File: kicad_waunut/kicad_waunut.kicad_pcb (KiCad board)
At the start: 2 copper layers, 129.3 x 265.9 mm, 76 parts, among them J1 Conn_01x06_Pin, J2 Conn_01x02_Pin, U1 ATtiny861A-S

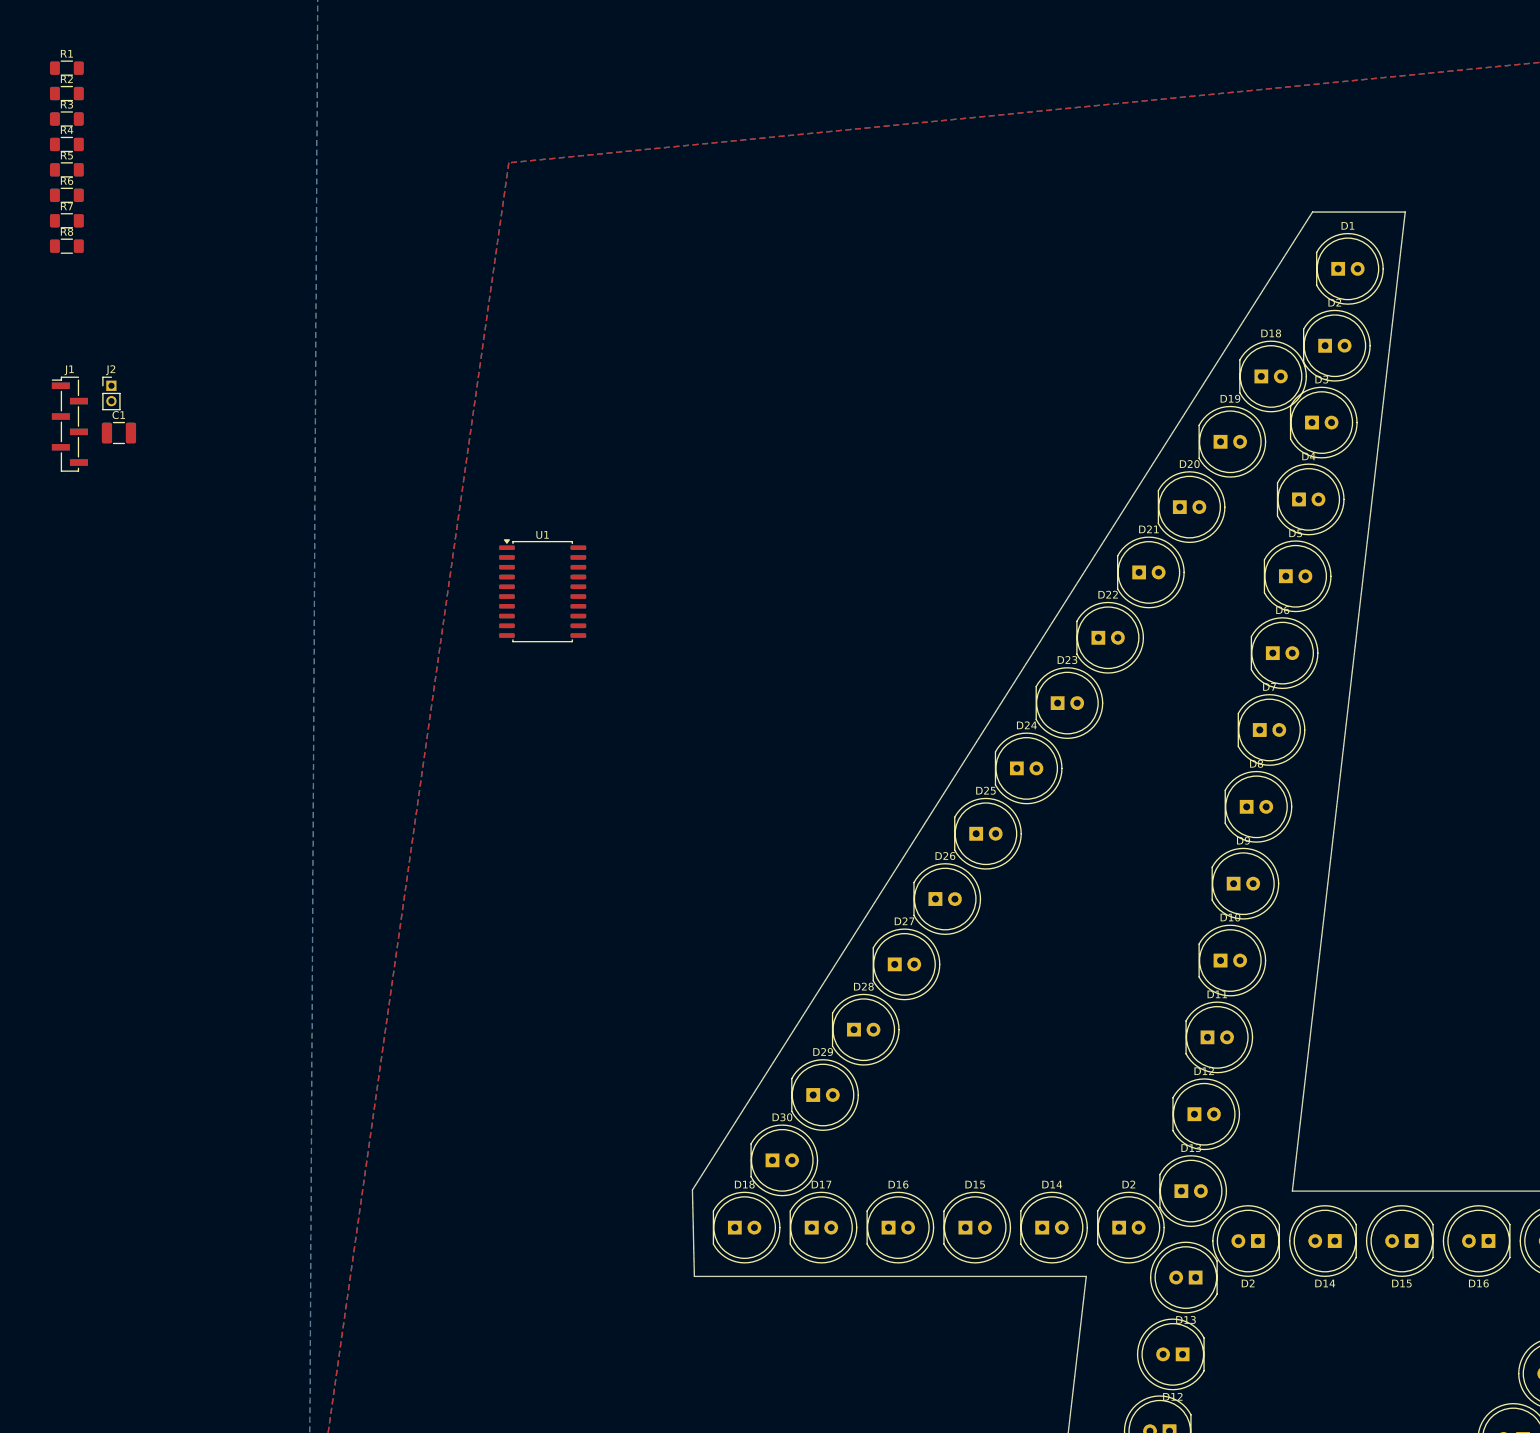
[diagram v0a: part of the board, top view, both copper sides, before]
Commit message: 2 lediä vilkkuu - vilkutus_2x.c
Jostain syystä kummallinen if statementti jossa 2 lediä palaa mutta eri
kirrkaudella.

Muutama ledi himmenee/kirkastuu. hmm...

Muuten jeba
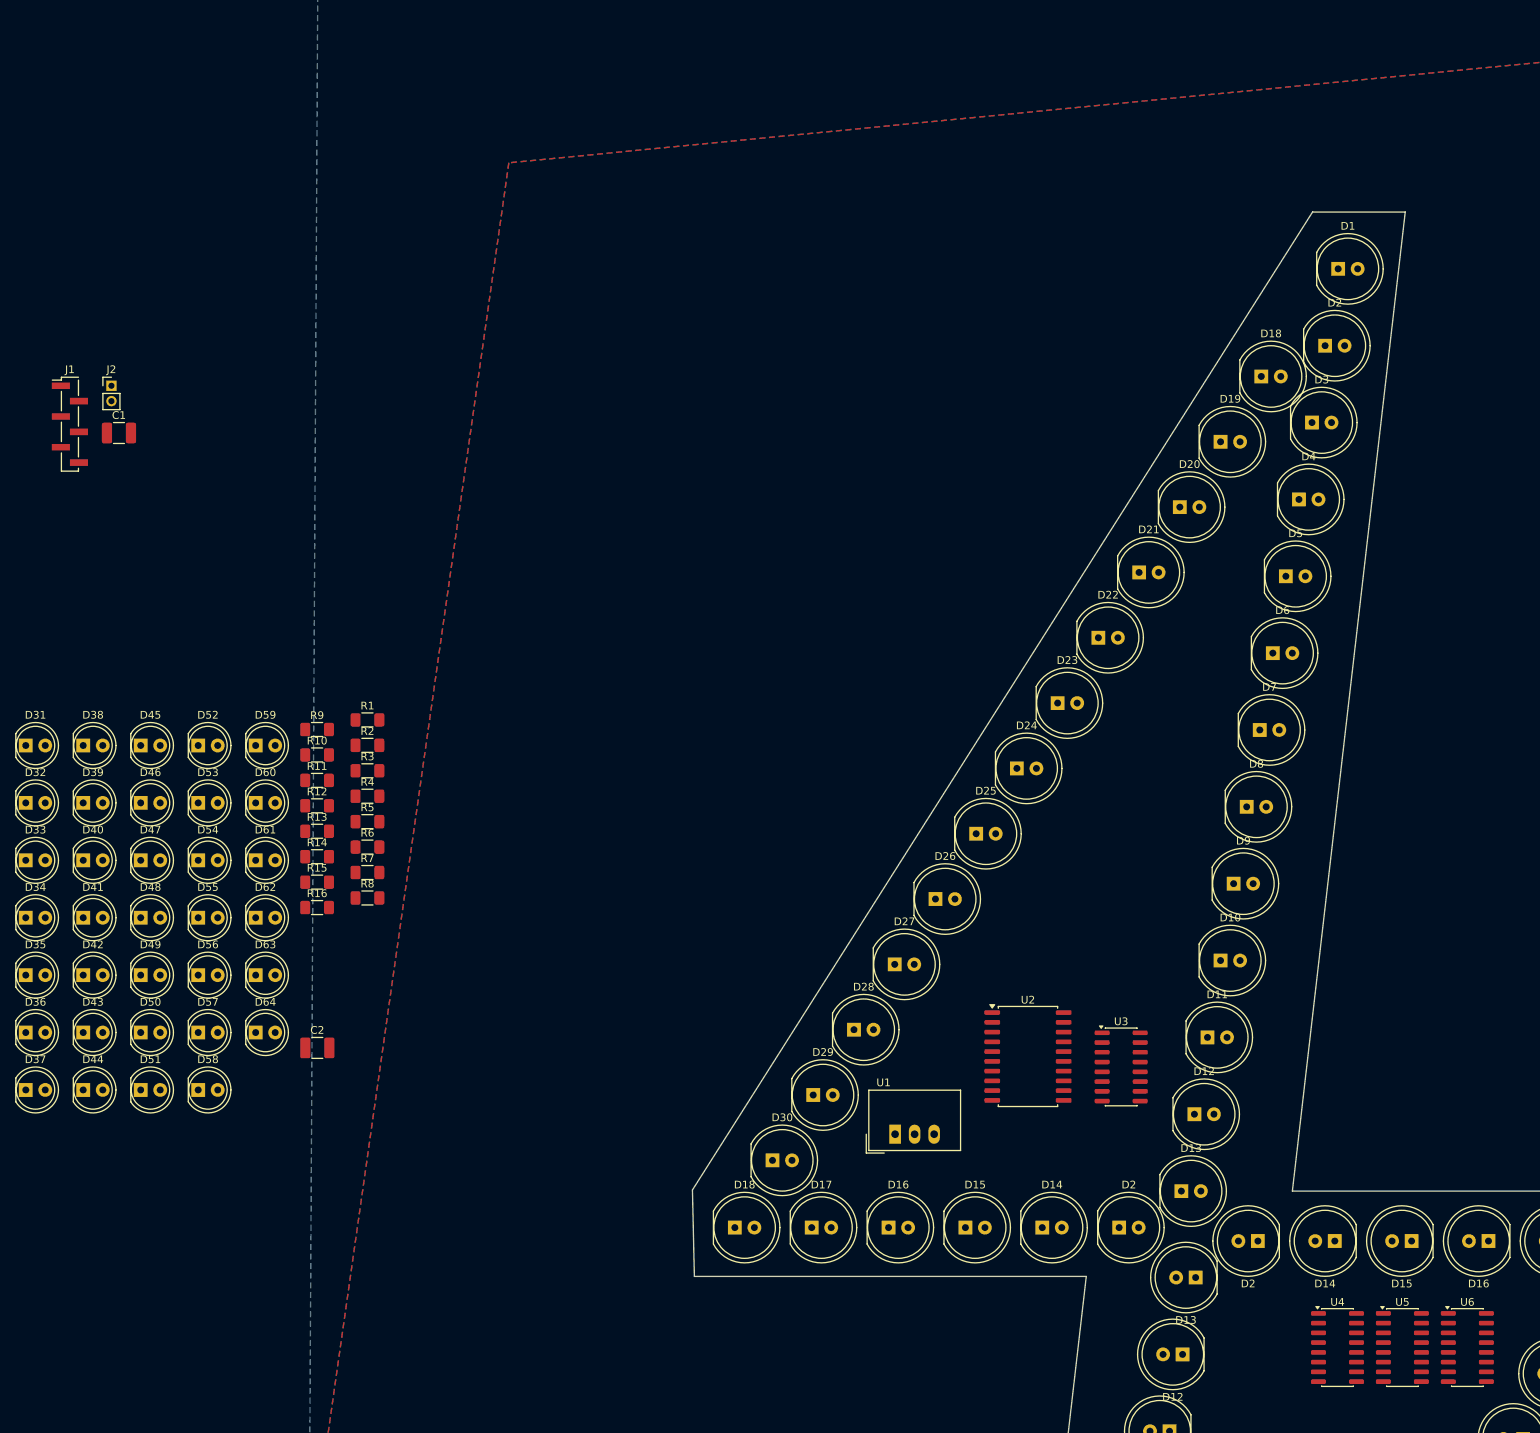
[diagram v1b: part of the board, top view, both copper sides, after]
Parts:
- added C2: 10 u, Capacitor_SMD:C_1210_3225Metric_Pad1.33x2.70mm_HandSolder, F.Cu at (15.9, 148.4)
- added D31: LED, LED_THT:LED_D5.0mm, F.Cu at (-22.1, 109.0)
- added D32: LED, LED_THT:LED_D5.0mm, F.Cu at (-22.1, 116.5)
- added D33: LED, LED_THT:LED_D5.0mm, F.Cu at (-22.1, 124.0)
- added D34: LED, LED_THT:LED_D5.0mm, F.Cu at (-22.1, 131.4)
- added D35: LED, LED_THT:LED_D5.0mm, F.Cu at (-22.1, 138.9)
- added D36: LED, LED_THT:LED_D5.0mm, F.Cu at (-22.1, 146.4)
- added D37: LED, LED_THT:LED_D5.0mm, F.Cu at (-22.1, 153.8)
- added D38: LED, LED_THT:LED_D5.0mm, F.Cu at (-14.6, 109.0)
- added D39: LED, LED_THT:LED_D5.0mm, F.Cu at (-14.6, 116.5)
- added D40: LED, LED_THT:LED_D5.0mm, F.Cu at (-14.6, 124.0)
- added D41: LED, LED_THT:LED_D5.0mm, F.Cu at (-14.6, 131.4)
- added D42: LED, LED_THT:LED_D5.0mm, F.Cu at (-14.6, 138.9)
- added D43: LED, LED_THT:LED_D5.0mm, F.Cu at (-14.6, 146.4)
- added D44: LED, LED_THT:LED_D5.0mm, F.Cu at (-14.6, 153.8)
- added D45: LED, LED_THT:LED_D5.0mm, F.Cu at (-7.10, 109.0)
- added D46: LED, LED_THT:LED_D5.0mm, F.Cu at (-7.10, 116.5)
- added D47: LED, LED_THT:LED_D5.0mm, F.Cu at (-7.10, 124.0)
- added D48: LED, LED_THT:LED_D5.0mm, F.Cu at (-7.10, 131.4)
- added D49: LED, LED_THT:LED_D5.0mm, F.Cu at (-7.10, 138.9)
- added D50: LED, LED_THT:LED_D5.0mm, F.Cu at (-7.10, 146.4)
- added D51: LED, LED_THT:LED_D5.0mm, F.Cu at (-7.10, 153.8)
- added D52: LED, LED_THT:LED_D5.0mm, F.Cu at (0.38, 109.0)
- added D53: LED, LED_THT:LED_D5.0mm, F.Cu at (0.38, 116.5)
- added D54: LED, LED_THT:LED_D5.0mm, F.Cu at (0.38, 124.0)
- added D55: LED, LED_THT:LED_D5.0mm, F.Cu at (0.38, 131.4)
- added D56: LED, LED_THT:LED_D5.0mm, F.Cu at (0.38, 138.9)
- added D57: LED, LED_THT:LED_D5.0mm, F.Cu at (0.38, 146.4)
- added D58: LED, LED_THT:LED_D5.0mm, F.Cu at (0.38, 153.8)
- added D59: LED, LED_THT:LED_D5.0mm, F.Cu at (7.86, 109.0)
- added D60: LED, LED_THT:LED_D5.0mm, F.Cu at (7.86, 116.5)
- added D61: LED, LED_THT:LED_D5.0mm, F.Cu at (7.86, 124.0)
- added D62: LED, LED_THT:LED_D5.0mm, F.Cu at (7.86, 131.4)
- added D63: LED, LED_THT:LED_D5.0mm, F.Cu at (7.86, 138.9)
- added D64: LED, LED_THT:LED_D5.0mm, F.Cu at (7.86, 146.4)
- added R10: 110, Resistor_SMD:R_1206_3216Metric_Pad1.30x1.75mm_HandSolder, F.Cu at (15.8, 110.2)
- added R11: 110, Resistor_SMD:R_1206_3216Metric_Pad1.30x1.75mm_HandSolder, F.Cu at (15.8, 113.6)
- added R12: 110, Resistor_SMD:R_1206_3216Metric_Pad1.30x1.75mm_HandSolder, F.Cu at (15.8, 116.9)
- added R13: 110, Resistor_SMD:R_1206_3216Metric_Pad1.30x1.75mm_HandSolder, F.Cu at (15.8, 120.2)
- added R14: 110, Resistor_SMD:R_1206_3216Metric_Pad1.30x1.75mm_HandSolder, F.Cu at (15.8, 123.5)
- added R15: 110, Resistor_SMD:R_1206_3216Metric_Pad1.30x1.75mm_HandSolder, F.Cu at (15.8, 126.8)
- added R16: 110, Resistor_SMD:R_1206_3216Metric_Pad1.30x1.75mm_HandSolder, F.Cu at (15.8, 130.1)
- added R9: 110, Resistor_SMD:R_1206_3216Metric_Pad1.30x1.75mm_HandSolder, F.Cu at (15.8, 106.9)
- added U2: ATtiny861A-S, Package_SO:SOIC-20W_7.5x12.8mm_P1.27mm, F.Cu at (108.3, 149.5)
- added U3: 74HC595, Package_SO:SOIC-16_3.9x9.9mm_P1.27mm, F.Cu at (120.5, 150.8)
- added U4: 74HC595, Package_SO:SOIC-16_3.9x9.9mm_P1.27mm, F.Cu at (148.6, 187.4)
- added U5: 74HC595, Package_SO:SOIC-16_3.9x9.9mm_P1.27mm, F.Cu at (157.1, 187.4)
- added U6: 74HC595, Package_SO:SOIC-16_3.9x9.9mm_P1.27mm, F.Cu at (165.5, 187.4)
- J1: value Conn_01x06_Pin -> Conn_01x02_Pin
- J2: value Conn_01x02_Pin -> Conn_01x06_Pin
- U1: value ATtiny861A-S -> TSR1-2450E; footprint Package_SO:SOIC-20W_7.5x12.8mm_P1.27mm -> Converter_DCDC:Converter_DCDC_TRACO_TSR-1_THT
- moved R8 93.4 mm to (22.4, 128.9)
- moved R1 93.4 mm to (22.4, 105.7)
- moved R2 93.4 mm to (22.4, 109.0)
- moved R3 93.4 mm to (22.4, 112.3)
- moved R4 93.4 mm to (22.4, 115.6)
- moved R5 93.4 mm to (22.4, 118.9)
- moved R6 93.4 mm to (22.4, 122.2)
- moved R7 93.4 mm to (22.4, 125.5)
- moved U1 84.2 mm to (91.1, 159.6)
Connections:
- D10 pad 1: Net-(D1-K) -> Net-(D10-K) (x2)
- D10 pad 2: Net-(D1-A) -> Net-(D10-A) (x2)
- D11 pad 1: Net-(D1-K) -> Net-(D11-K) (x2)
- D11 pad 2: Net-(D1-A) -> Net-(D10-A) (x2)
- D12 pad 1: Net-(D1-K) -> Net-(D12-K) (x2)
- D12 pad 2: Net-(D1-A) -> Net-(D10-A) (x2)
- D13 pad 2: Net-(D1-A) -> Net-(D13-A) (x2)
- D14 pad 1: (no net) -> Net-(D10-K) (x2)
- D14 pad 2: (no net) -> Net-(D13-A) (x2)
- D15 pad 1: (no net) -> Net-(D11-K) (x2)
- D15 pad 2: (no net) -> Net-(D13-A) (x2)
- D16 pad 1: (no net) -> Net-(D12-K) (x2)
- D16 pad 2: (no net) -> Net-(D13-A) (x2)
- D17 pad 1: (no net) -> Net-(D17-K) (x2)
- D17 pad 2: (no net) -> Net-(D17-A) (x2)
- D18 pad 1: (no net) -> Net-(D17-K) (x4)
- D18 pad 2: (no net) -> Net-(D18-A) (x4)
- D19 pad 1: (no net) -> Net-(D17-K) (x2)
- D19 pad 2: (no net) -> Net-(D19-A) (x2)
- D2 pad 1: Net-(D1-K) -> Net-(D10-K) (x2)
- D2 pad 1: (no net) -> Net-(D10-K) (x2)
- D2 pad 2: (no net) -> Net-(D1-A) (x2)
- D20 pad 1: (no net) -> Net-(D17-K) (x2)
- D20 pad 2: (no net) -> Net-(D20-A) (x2)
- D21 pad 1: (no net) -> Net-(D21-K) (x2)
- D21 pad 2: (no net) -> Net-(D17-A) (x2)
- D22 pad 1: (no net) -> Net-(D21-K) (x2)
- D22 pad 2: (no net) -> Net-(D18-A) (x2)
- D23 pad 1: (no net) -> Net-(D21-K) (x2)
- D23 pad 2: (no net) -> Net-(D19-A) (x2)
- D24 pad 1: (no net) -> Net-(D21-K) (x2)
- D24 pad 2: (no net) -> Net-(D20-A) (x2)
- D25 pad 1: (no net) -> Net-(D25-K) (x2)
- D25 pad 2: (no net) -> Net-(D17-A) (x2)
- D26 pad 1: (no net) -> Net-(D25-K) (x2)
- D26 pad 2: (no net) -> Net-(D18-A) (x2)
- D27 pad 1: (no net) -> Net-(D25-K) (x2)
- D27 pad 2: (no net) -> Net-(D19-A) (x2)
- D28 pad 1: (no net) -> Net-(D25-K) (x2)
- D28 pad 2: (no net) -> Net-(D20-A) (x2)
- D29 pad 1: (no net) -> Net-(D29-K) (x2)
- D29 pad 2: (no net) -> Net-(D17-A) (x2)
- D3 pad 1: Net-(D1-K) -> Net-(D11-K) (x2)
- D30 pad 1: (no net) -> Net-(D29-K) (x2)
- D30 pad 2: (no net) -> Net-(D18-A) (x2)
- D4 pad 1: Net-(D1-K) -> Net-(D12-K) (x2)
- D5 pad 2: Net-(D1-A) -> Net-(D5-A) (x2)
- D6 pad 1: Net-(D1-K) -> Net-(D10-K) (x2)
- D6 pad 2: Net-(D1-A) -> Net-(D5-A) (x2)
- D7 pad 1: Net-(D1-K) -> Net-(D11-K) (x2)
- D7 pad 2: Net-(D1-A) -> Net-(D5-A) (x2)
- D8 pad 1: Net-(D1-K) -> Net-(D12-K) (x2)
- D8 pad 2: Net-(D1-A) -> Net-(D5-A) (x2)
- D9 pad 2: Net-(D1-A) -> Net-(D10-A) (x2)
- J1 pad 1: Net-(D1-K) -> Net-(J1-Pin_1)
- J1 pad 2: Net-(D10-K) -> GND
- J1 pad 3: Net-(D11-K) -> (no net)
- J1 pad 4: +5V -> (no net)
- J1 pad 5: GND -> (no net)
- J1 pad 6: Net-(D16-K) -> (no net)
- J2 pad 1: +5V -> Net-(J2-Pin_1)
- J2 pad 2: GND -> Net-(J2-Pin_2)
- R1 pad 1: Net-(U1-PA0) -> Net-(U3-QA)
- R2 pad 1: Net-(U1-PA1) -> Net-(U3-QB)
- R2 pad 2: Net-(D10-A) -> Net-(D5-A)
- R3 pad 1: Net-(U1-PA2) -> Net-(U3-QC)
- R3 pad 2: Net-(D17-A) -> Net-(D10-A)
- R4 pad 1: Net-(U1-AREF/PA3) -> Net-(U3-QD)
- R4 pad 2: Net-(D25-A) -> Net-(D13-A)
- R5 pad 1: Net-(U1-PA4) -> Net-(U4-QA)
- R5 pad 2: Net-(D33-A) -> Net-(D17-A)
- R6 pad 1: Net-(U1-PA5) -> Net-(U4-QB)
- R6 pad 2: Net-(D41-A) -> Net-(D18-A)
- R7 pad 1: Net-(U1-PA6) -> Net-(U4-QC)
- R7 pad 2: Net-(D49-A) -> Net-(D19-A)
- R8 pad 1: Net-(U1-PA7) -> Net-(U4-QD)
- R8 pad 2: Net-(D57-A) -> Net-(D20-A)
- U1 pad 1: Net-(D1-K) -> Net-(J1-Pin_1)
- U1 pad 2: Net-(D10-K) -> GND
- U1 pad 3: Net-(D11-K) -> +5V

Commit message: Waunujen skemaa muutettu. README tiedostoja päivitetty.
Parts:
- removed U3, U4, U5, U6: 74HC595, Package_SO:SOIC-16_3.9x9.9mm_P1.27mm
- added Q1: NPN, Package_TO_SOT_SMD:SOT-23, F.Cu at (55.7, 189.6)
- added Q2: NPN, Package_TO_SOT_SMD:SOT-23, F.Cu at (55.7, 194.0)
- added Q3: NPN, Package_TO_SOT_SMD:SOT-23, F.Cu at (60.6, 189.6)
- added Q4: NPN, Package_TO_SOT_SMD:SOT-23, F.Cu at (60.6, 194.0)
- added Q5: NPN, Package_TO_SOT_SMD:SOT-23, F.Cu at (65.6, 189.6)
- added Q6: NPN, Package_TO_SOT_SMD:SOT-23, F.Cu at (65.6, 194.0)
- added Q7: NPN, Package_TO_SOT_SMD:SOT-23, F.Cu at (70.5, 189.6)
- added Q8: NPN, Package_TO_SOT_SMD:SOT-23, F.Cu at (70.5, 194.0)
- J1: footprint Connector_PinHeader_2.00mm:PinHeader_1x06_P2.00mm_Vertical_SMD_Pin1Left -> Connector_PinHeader_2.00mm:PinHeader_1x02_P2.00mm_Vertical
- J2: footprint Connector_PinHeader_2.00mm:PinHeader_1x02_P2.00mm_Vertical -> Connector_PinHeader_2.00mm:PinHeader_1x06_P2.00mm_Vertical_SMD_Pin1Left
- R10, R11, R12, R13, R14, R15, R16, R9: value 110 -> 1000
- moved J1 121.1 mm to (54.1, 165.8)
- moved J2 121.1 mm to (42.6, 170.8)
- moved C1 114.0 mm to (49.0, 165.9)
- moved R10 55.6 mm to (48.2, 155.5)
- moved R11 55.6 mm to (48.2, 158.8)
- moved R12 55.6 mm to (48.2, 162.1)
- moved R9 55.6 mm to (48.2, 152.2)
- moved D31 46.8 mm to (4.34, 147.7)
- moved D32 46.8 mm to (4.34, 155.1)
- moved D33 46.8 mm to (4.34, 162.6)
- moved D38 46.8 mm to (11.8, 147.7)
- moved D39 46.8 mm to (11.8, 155.1)
- moved D40 46.8 mm to (11.8, 162.6)
- moved D45 46.8 mm to (19.3, 147.7)
- moved D46 46.8 mm to (19.3, 155.1)
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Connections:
- net Net-(J1-Pin_1) renamed +12V
- D11 pad 1: Net-(D11-K) -> Net-(D10-K) (x2)
- D11 pad 2: Net-(D10-A) -> Net-(D11-A) (x2)
- D12 pad 1: Net-(D12-K) -> Net-(D10-K) (x2)
- D12 pad 2: Net-(D10-A) -> Net-(D12-A) (x2)
- D13 pad 1: Net-(D1-K) -> Net-(D10-K) (x2)
- D14 pad 2: Net-(D13-A) -> Net-(D14-A) (x2)
- D15 pad 1: Net-(D11-K) -> Net-(D10-K) (x2)
- D15 pad 2: Net-(D13-A) -> Net-(D15-A) (x2)
- D16 pad 1: Net-(D12-K) -> Net-(D10-K) (x2)
- D16 pad 2: Net-(D13-A) -> Net-(D16-A) (x2)
- D17 pad 2: Net-(D17-A) -> Net-(D1-A) (x2)
- D18 pad 2: Net-(D18-A) -> Net-(D10-A) (x4)
- D19 pad 2: Net-(D19-A) -> Net-(D11-A) (x2)
- D2 pad 1: Net-(D10-K) -> Net-(D1-K) (x4)
- D2 pad 2: Net-(D1-A) -> Net-(D10-A) (x4)
- D20 pad 2: Net-(D20-A) -> Net-(D12-A) (x2)
- D21 pad 1: Net-(D21-K) -> Net-(D17-K) (x2)
- D21 pad 2: Net-(D17-A) -> Net-(D13-A) (x2)
- D22 pad 1: Net-(D21-K) -> Net-(D17-K) (x2)
- D22 pad 2: Net-(D18-A) -> Net-(D14-A) (x2)
- D23 pad 1: Net-(D21-K) -> Net-(D17-K) (x2)
- D23 pad 2: Net-(D19-A) -> Net-(D15-A) (x2)
- D24 pad 1: Net-(D21-K) -> Net-(D17-K) (x2)
- D24 pad 2: Net-(D20-A) -> Net-(D16-A) (x2)
- D25 pad 2: Net-(D17-A) -> Net-(D1-A) (x2)
- D26 pad 2: Net-(D18-A) -> Net-(D10-A) (x2)
- D27 pad 2: Net-(D19-A) -> Net-(D11-A) (x2)
- D28 pad 2: Net-(D20-A) -> Net-(D12-A) (x2)
- D29 pad 1: Net-(D29-K) -> Net-(D25-K) (x2)
- D29 pad 2: Net-(D17-A) -> Net-(D13-A) (x2)
- D3 pad 1: Net-(D11-K) -> Net-(D1-K) (x2)
- D3 pad 2: Net-(D1-A) -> Net-(D11-A) (x2)
- D30 pad 1: Net-(D29-K) -> Net-(D25-K) (x2)
- D30 pad 2: Net-(D18-A) -> Net-(D14-A) (x2)
- D31 pad 1: Net-(D29-K) -> Net-(D25-K)
- D31 pad 2: Net-(D19-A) -> Net-(D15-A)
- D32 pad 1: Net-(D29-K) -> Net-(D25-K)
- D32 pad 2: Net-(D20-A) -> Net-(D16-A)
- D33 pad 2: Net-(D33-A) -> Net-(D1-A)
- D34 pad 2: Net-(D34-A) -> Net-(D10-A)
- D35 pad 2: Net-(D35-A) -> Net-(D11-A)
- D36 pad 2: Net-(D36-A) -> Net-(D12-A)
- D37 pad 1: Net-(D37-K) -> Net-(D33-K)
- D37 pad 2: Net-(D33-A) -> Net-(D13-A)
- D38 pad 1: Net-(D37-K) -> Net-(D33-K)
- D38 pad 2: Net-(D34-A) -> Net-(D14-A)
- D39 pad 1: Net-(D37-K) -> Net-(D33-K)
- D39 pad 2: Net-(D35-A) -> Net-(D15-A)
- D4 pad 1: Net-(D12-K) -> Net-(D1-K) (x2)
- D4 pad 2: Net-(D1-A) -> Net-(D12-A) (x2)
- D40 pad 1: Net-(D37-K) -> Net-(D33-K)
- D40 pad 2: Net-(D36-A) -> Net-(D16-A)
- D41 pad 2: Net-(D33-A) -> Net-(D1-A)
- D42 pad 2: Net-(D34-A) -> Net-(D10-A)
- D43 pad 2: Net-(D35-A) -> Net-(D11-A)
- D44 pad 2: Net-(D36-A) -> Net-(D12-A)
- D45 pad 1: Net-(D45-K) -> Net-(D41-K)
- D45 pad 2: Net-(D33-A) -> Net-(D13-A)
- D46 pad 1: Net-(D45-K) -> Net-(D41-K)
- D46 pad 2: Net-(D34-A) -> Net-(D14-A)
- D47 pad 1: Net-(D45-K) -> Net-(D41-K)
- D47 pad 2: Net-(D35-A) -> Net-(D15-A)
- D48 pad 1: Net-(D45-K) -> Net-(D41-K)
- D48 pad 2: Net-(D36-A) -> Net-(D16-A)
- D49 pad 2: Net-(D49-A) -> Net-(D1-A)
- D5 pad 2: Net-(D5-A) -> Net-(D13-A) (x2)
- D50 pad 2: Net-(D50-A) -> Net-(D10-A)
- D51 pad 2: Net-(D51-A) -> Net-(D11-A)
- D52 pad 2: Net-(D52-A) -> Net-(D12-A)
- D53 pad 1: Net-(D53-K) -> Net-(D49-K)
- D53 pad 2: Net-(D49-A) -> Net-(D13-A)
- D54 pad 1: Net-(D53-K) -> Net-(D49-K)
- D54 pad 2: Net-(D50-A) -> Net-(D14-A)
- D55 pad 1: Net-(D53-K) -> Net-(D49-K)
- D55 pad 2: Net-(D51-A) -> Net-(D15-A)
- D56 pad 1: Net-(D53-K) -> Net-(D49-K)
- D56 pad 2: Net-(D52-A) -> Net-(D16-A)
- D57 pad 2: Net-(D49-A) -> Net-(D1-A)
- D58 pad 2: Net-(D50-A) -> Net-(D10-A)
- D59 pad 2: Net-(D51-A) -> Net-(D11-A)
- D6 pad 1: Net-(D10-K) -> Net-(D1-K) (x2)
- D6 pad 2: Net-(D5-A) -> Net-(D14-A) (x2)
- D60 pad 2: Net-(D52-A) -> Net-(D12-A)
- D61 pad 1: Net-(D61-K) -> Net-(D57-K)
- D61 pad 2: Net-(D49-A) -> Net-(D13-A)
- D62 pad 1: Net-(D61-K) -> Net-(D57-K)
- D62 pad 2: Net-(D50-A) -> Net-(D14-A)
- D63 pad 1: Net-(D61-K) -> Net-(D57-K)
- D63 pad 2: Net-(D51-A) -> Net-(D15-A)
- D64 pad 1: Net-(D61-K) -> Net-(D57-K)
- D64 pad 2: Net-(D52-A) -> Net-(D16-A)
- D7 pad 1: Net-(D11-K) -> Net-(D1-K) (x2)
- D7 pad 2: Net-(D5-A) -> Net-(D15-A) (x2)
- D8 pad 1: Net-(D12-K) -> Net-(D1-K) (x2)
- D8 pad 2: Net-(D5-A) -> Net-(D16-A) (x2)
- D9 pad 1: Net-(D1-K) -> Net-(D10-K) (x2)
- D9 pad 2: Net-(D10-A) -> Net-(D1-A) (x2)
- R1 pad 1: Net-(U3-QA) -> Net-(U2-PA0)
- R10 pad 1: Net-(U5-QB) -> Net-(J2-Pin_2)
- R10 pad 2: Net-(D34-A) -> Net-(Q2-B)
- R11 pad 1: Net-(U5-QC) -> Net-(J2-Pin_3)
- R11 pad 2: Net-(D35-A) -> Net-(Q3-B)
- R12 pad 1: Net-(U5-QD) -> Net-(U2-PB3)
- R12 pad 2: Net-(D36-A) -> Net-(Q4-B)
- R13 pad 1: Net-(U6-QA) -> Net-(U2-XTAL1/PB4)
- R13 pad 2: Net-(D49-A) -> Net-(Q5-B)
- R14 pad 1: Net-(U6-QB) -> Net-(U2-XTAL2/PB5)
- R14 pad 2: Net-(D50-A) -> Net-(Q6-B)
- R15 pad 1: Net-(U6-QC) -> Net-(U2-PB6)
- R15 pad 2: Net-(D51-A) -> Net-(Q7-B)
- R16 pad 1: Net-(U6-QD) -> Net-(J2-Pin_6)
- R16 pad 2: Net-(D52-A) -> Net-(Q8-B)
- R2 pad 1: Net-(U3-QB) -> Net-(U2-PA1)
- R2 pad 2: Net-(D5-A) -> Net-(D10-A)
- R3 pad 1: Net-(U3-QC) -> Net-(U2-PA2)
- R3 pad 2: Net-(D10-A) -> Net-(D11-A)
- R4 pad 1: Net-(U3-QD) -> Net-(U2-AREF/PA3)
- R4 pad 2: Net-(D13-A) -> Net-(D12-A)
- R5 pad 1: Net-(U4-QA) -> Net-(U2-PA4)
- R5 pad 2: Net-(D17-A) -> Net-(D13-A)
- R6 pad 1: Net-(U4-QB) -> Net-(U2-PA5)
- R6 pad 2: Net-(D18-A) -> Net-(D14-A)
- R7 pad 1: Net-(U4-QC) -> Net-(U2-PA6)
- R7 pad 2: Net-(D19-A) -> Net-(D15-A)
- R8 pad 1: Net-(U4-QD) -> Net-(U2-PA7)
- R8 pad 2: Net-(D20-A) -> Net-(D16-A)
- R9 pad 1: Net-(U5-QA) -> Net-(J2-Pin_1)
- R9 pad 2: Net-(D33-A) -> Net-(Q1-B)
- U2 pad 11: unconnected-(U2-PA7-Pad11) -> Net-(U2-PA7)
- U2 pad 12: unconnected-(U2-PA6-Pad12) -> Net-(U2-PA6)
- U2 pad 13: unconnected-(U2-PA5-Pad13) -> Net-(U2-PA5)
- U2 pad 17: unconnected-(U2-AREF/PA3-Pad17) -> Net-(U2-AREF/PA3)
- U2 pad 4: unconnected-(U2-PB3-Pad4) -> Net-(U2-PB3)
- U2 pad 7: unconnected-(U2-XTAL1/PB4-Pad7) -> Net-(U2-XTAL1/PB4)
- U2 pad 8: unconnected-(U2-XTAL2/PB5-Pad8) -> Net-(U2-XTAL2/PB5)
- U2 pad 9: unconnected-(U2-PB6-Pad9) -> Net-(U2-PB6)
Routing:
- removed copper zone on B.Cu, net (none)
- removed copper zone on B.Cu, net GND
- removed copper zone on F.Cu, net GND
